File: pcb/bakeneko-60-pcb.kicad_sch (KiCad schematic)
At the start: 18 parts

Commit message: add fn1
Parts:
- C1, C2, C3: value (none) -> 0.1u; footprint (none) -> Capacitor_SMD:C_0805_2012Metric
- C4: value (none) -> 10u; footprint (none) -> Capacitor_SMD:C_0805_2012Metric
- C5, C7: value (none) -> 22p; footprint (none) -> Capacitor_SMD:C_0805_2012Metric
- C6: value (none) -> 1u; footprint (none) -> Capacitor_SMD:C_0805_2012Metric
- F1: value (none) -> 500mA; footprint (none) -> Fuse:Fuse_1206_3216Metric
- J1: value (none) -> JST SH 4-pin; footprint (none) -> Connector_JST:JST_SH_SM04B-SRSS-TB_1x04-1MP_P1.00mm_Horizontal
- J2: value (none) -> AVR-ISP-6; footprint (none) -> bakeneko:ISP
- R1, R2: value (none) -> 22; footprint (none) -> Resistor_SMD:R_0805_2012Metric
- R3, R4: value (none) -> 10k; footprint (none) -> Resistor_SMD:R_0805_2012Metric
- SW1: value (none) -> Reset; footprint (none) -> Button_Switch_SMD:SW_SPST_TL3342
- U1: value (none) -> SRV05-4; footprint (none) -> Package_TO_SOT_SMD:SOT-23-6
- U2: value (none) -> ATmega32U4-AU; footprint (none) -> Package_QFP:TQFP-44_10x10mm_P0.8mm
- Y1: value (none) -> 16MHz; footprint (none) -> Crystal:Crystal_SMD_3225-4Pin_3.2x2.5mm

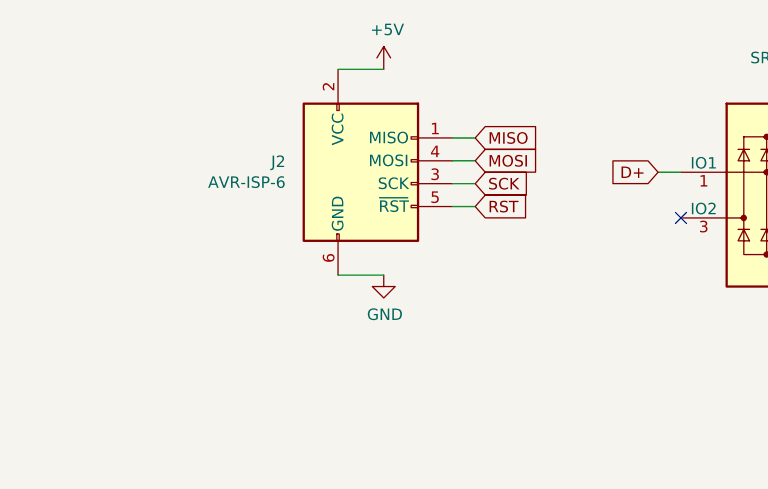
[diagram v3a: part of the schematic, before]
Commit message: remove isp
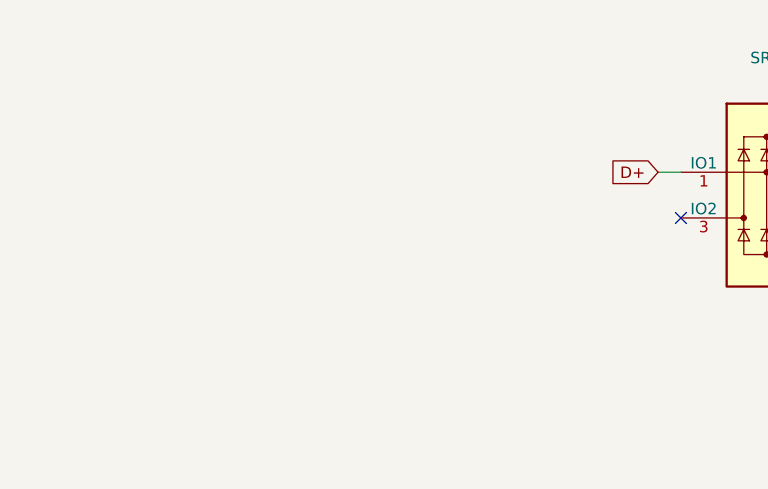
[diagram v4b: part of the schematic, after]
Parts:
- removed J2: AVR-ISP-6, bakeneko:ISP, symbol Connector:AVR-ISP-6
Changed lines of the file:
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@@
-    (stroke (width 0) (type default) (color 0 0 0 0))
-  )
-  (wire (pts (xy 68.58 36.83) (xy 71.12 36.83))
-    (stroke (width 0) (type default) (color 0 0 0 0))
-  )
-  (wire (pts (xy 71.12 39.37) (xy 68.58 39.37))
     (stroke (width 0) (type default) (color 0 0 0 0))
   )
@@
     (stroke (width 0) (type default) (color 0 0 0 0))
   )
-  (wire (pts (xy 60.96 29.21) (xy 55.88 29.21))
-    (stroke (width 0) (type default) (color 0 0 0 0))
-  )
   (wire (pts (xy 130.81 88.9) (xy 140.97 88.9))
     (stroke (width 0) (type default) (color 0 0 0 0))
@@
     (stroke (width 0) (type default) (color 0 0 0 0))
   )
-  (wire (pts (xy 68.58 41.91) (xy 71.12 41.91))
-    (stroke (width 0) (type default) (color 0 0 0 0))
-  )
   (wire (pts (xy 81.28 163.83) (xy 78.74 163.83))
     (stroke (width 0) (type default) (color 0 0 0 0))
@@
     (stroke (width 0) (type default) (color 0 0 0 0))
   )
-  (wire (pts (xy 55.88 52.07) (xy 60.96 52.07))
-    (stroke (width 0) (type default) (color 0 0 0 0))
-  )
   (wire (pts (xy 78.74 130.81) (xy 81.28 130.81))
     (stroke (width 0) (type default) (color 0 0 0 0))
@@
   )
   (wire (pts (xy 81.28 148.59) (xy 78.74 148.59))
-    (stroke (width 0) (type default) (color 0 0 0 0))
-  )
-  (wire (pts (xy 71.12 44.45) (xy 68.58 44.45))
     (stroke (width 0) (type default) (color 0 0 0 0))
   )
@@
     )
   )
-  (global_label "SCK" (shape input) (at 71.12 41.91 0) (fields_autoplaced)
-    (effects (font (size 1.27 1.27)) (justify left))
-    (property "Intersheet References" "${INTERSHEET_REFS}" (id 0) (at 0 0 0)
-      (effects (font (size 1.27 1.27)) hide)
-    )
-  )
-  (global_label "MISO" (shape input) (at 71.12 36.83 0) (fields_autoplaced)
-    (effects (font (size 1.27 1.27)) (justify left))
-    (property "Intersheet References" "${INTERSHEET_REFS}" (id 0) (at 0 0 0)
-      (effects (font (size 1.27 1.27)) hide)
-    )
-  )
-  (global_label "RST" (shape input) (at 71.12 44.45 0) (fields_autoplaced)
-    (effects (font (size 1.27 1.27)) (justify left))
-    (property "Intersheet References" "${INTERSHEET_REFS}" (id 0) (at 0 0 0)
-      (effects (font (size 1.27 1.27)) hide)
-    )
-  )
   (global_label "D-" (shape input) (at 144.78 36.83 180) (fields_autoplaced)
     (effects (font (size 1.27 1.27)) (justify right))
@@
   )
   (global_label "COL13" (shape input) (at 81.28 128.27 0) (fields_autoplaced)
-    (effects (font (size 1.27 1.27)) (justify left))
-    (property "Intersheet References" "${INTERSHEET_REFS}" (id 0) (at 0 0 0)
-      (effects (font (size 1.27 1.27)) hide)
-    )
-  )
-  (global_label "MOSI" (shape input) (at 71.12 39.37 0) (fields_autoplaced)
     (effects (font (size 1.27 1.27)) (justify left))
     (property "Intersheet References" "${INTERSHEET_REFS}" (id 0) (at 0 0 0)
@@
     (pin "1")
   )
-  (symbol (lib_id "power:+5V") (at 60.96 29.21 0) (unit 1)
-    (in_bom yes) (on_board yes)
-    (property "Reference" "#PWR01" (id 0) (at 60.96 33.02 0)
-      (effects (font (size 1.27 1.27)) hide)
-    )
-    (property "Value" "+5V" (id 1) (at 61.341 24.8158 0))
-    (property "Footprint" "" (id 2) (at 60.96 29.21 0)
-      (effects (font (size 1.27 1.27)) hide)
-    )
-    (property "Datasheet" "" (id 3) (at 60.96 29.21 0)
-      (effects (font (size 1.27 1.27)) hide)
-    )
-    (pin "1")
-  )
   (symbol (lib_id "power:+5V") (at 129.54 163.83 0) (unit 1)
     (in_bom yes) (on_board yes)
@@
     )
     (property "Datasheet" "" (id 3) (at 60.96 82.55 0)
-      (effects (font (size 1.27 1.27)) hide)
-    )
-    (pin "1")
-  )
-  (symbol (lib_id "Connector:AVR-ISP-6") (at 58.42 41.91 0) (unit 1)
-    (in_bom yes) (on_board yes)
-    (property "Reference" "J2" (id 0) (at 50.0634 39.4716 0)
-      (effects (font (size 1.27 1.27)) (justify right))
-    )
-    (property "Value" "AVR-ISP-6" (id 1) (at 50.0634 41.783 0)
-      (effects (font (size 1.27 1.27)) (justify right))
-    )
-    (property "Footprint" "bakeneko:ISP" (id 2) (at 52.07 40.64 90)
-      (effects (font (size 1.27 1.27)) hide)
-    )
-    (property "Datasheet" " ~" (id 3) (at 26.035 55.88 0)
-      (effects (font (size 1.27 1.27)) hide)
-    )
-    (pin "1")
-    (pin "2")
-    (pin "3")
-    (pin "4")
-    (pin "5")
-    (pin "6")
-  )
-  (symbol (lib_id "power:GND") (at 60.96 52.07 0) (unit 1)
-    (in_bom yes) (on_board yes)
-    (property "Reference" "#PWR08" (id 0) (at 60.96 58.42 0)
-      (effects (font (size 1.27 1.27)) hide)
-    )
-    (property "Value" "GND" (id 1) (at 61.087 56.4642 0))
-    (property "Footprint" "" (id 2) (at 60.96 52.07 0)
-      (effects (font (size 1.27 1.27)) hide)
-    )
-    (property "Datasheet" "" (id 3) (at 60.96 52.07 0)
       (effects (font (size 1.27 1.27)) hide)
     )
@@
       (reference "#FLG03") (unit 1) (value "PWR_FLAG") (footprint "")
     )
-    (path "/00000000-0000-0000-0000-00005f3d1a13"
-      (reference "#PWR01") (unit 1) (value "+5V") (footprint "")
-    )
     (path "/00000000-0000-0000-0000-00005f275d18"
       (reference "#PWR03") (unit 1) (value "VBUS") (footprint "")
@@
       (reference "#PWR07") (unit 1) (value "GND") (footprint "")
     )
-    (path "/00000000-0000-0000-0000-00005f4d2bf6"
-      (reference "#PWR08") (unit 1) (value "GND") (footprint "")
-    )
     (path "/00000000-0000-0000-0000-00005f277a1c"
       (reference "#PWR010") (unit 1) (value "VBUS") (footprint "")
@@
       (reference "J1") (unit 1) (value "JST SH 4-pin") (footprint "Connector_JST:JST_SH_SM04B-SRSS-TB_1x04-1MP_P1.00mm_Horizontal")
     )
-    (path "/00000000-0000-0000-0000-00005f4c9cce"
-      (reference "J2") (unit 1) (value "AVR-ISP-6") (footprint "bakeneko:ISP")
-    )
     (path "/00000000-0000-0000-0000-00005f45b9b8/00000000-0000-0000-0000-00005f497539"
